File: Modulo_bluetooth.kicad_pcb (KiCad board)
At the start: 2 copper layers, 0 parts

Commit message: Layout terminado
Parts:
- added C1: 470p, Capacitors_SMD:C_0805_HandSoldering, F.Cu at (158.4, 133.3)
- added C2: 100n, Capacitors_SMD:C_0805_HandSoldering, F.Cu at (150.6, 132.5)
- added C3: 1u, Capacitors_SMD:C_0805_HandSoldering, F.Cu at (150.6, 134.6)
- added D1: 1N5817, w_smd_diode:do214ac, F.Cu at (156.1, 139.3)
- added D2: LED, LEDs:LED_0805, F.Cu at (161.7, 132.3)
- added P1: CONN_01X06, Pin_Headers:Pin_Header_Angled_1x06, F.Cu at (162.7, 142.2)
- added R1: 41k, Resistors_SMD:R_0805_HandSoldering, F.Cu at (162.1, 136.8)
- added R2: 220k, Resistors_SMD:R_0805_HandSoldering, F.Cu at (155.6, 136.8)
- added R3: 10k, Resistors_SMD:R_0805_HandSoldering, F.Cu at (162.1, 138.9)
- added R4: 2k, Resistors_SMD:R_0805_HandSoldering, F.Cu at (162.1, 134.6)
- added SW1: SW_Push, Buttons_Switches_SMD:SW_SPST_B3U-1000P-B, F.Cu at (150.6, 138.2)
- added U1: HC-05, IFS-BoB:HC-06, F.Cu at (156.3, 116.3)
- added U2: MIC5219-3.3BM5, TO_SOT_Packages_SMD:SOT-23-5, F.Cu at (155.3, 133.5)
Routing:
- net Net-(R3-Pad2): track 0.00 -> 55.8 mm, vias 0 -> 4
- net GND: track 0.00 -> 51.8 mm, vias 0 -> 6
- net STATE: track 0.00 -> 38.6 mm, vias 0 -> 1
- net TXD: track 0.00 -> 36.1 mm, vias 0 -> 1
- net RXD: track 0.00 -> 34.2 mm, vias 0 -> 1
- net Net-(R4-Pad2): track 0.00 -> 24.9 mm, vias 0 -> 2
- net +3V3: track 0.00 -> 18.8 mm
- net EN: track 0.00 -> 7.43 mm
- net Net-(R1-Pad1): track 0.00 -> 6.25 mm
- net Net-(D1-Pad1): track 0.00 -> 4.86 mm
- net +5V: track 0.00 -> 3.92 mm
- net Net-(D2-Pad2): track 0.00 -> 2.34 mm
- net Net-(C1-Pad1): track 0.00 -> 2.21 mm
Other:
- board outline added: 18.2 x 36.3 mm

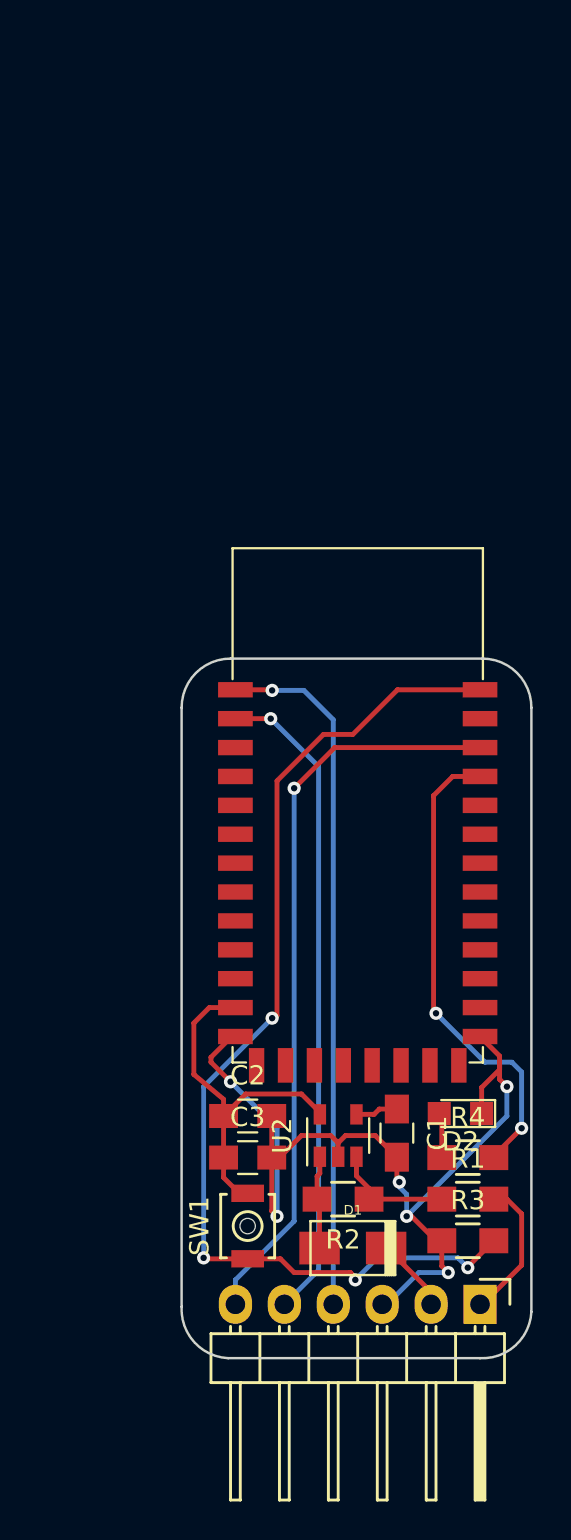
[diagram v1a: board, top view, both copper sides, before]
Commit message: Serigrafia añadida
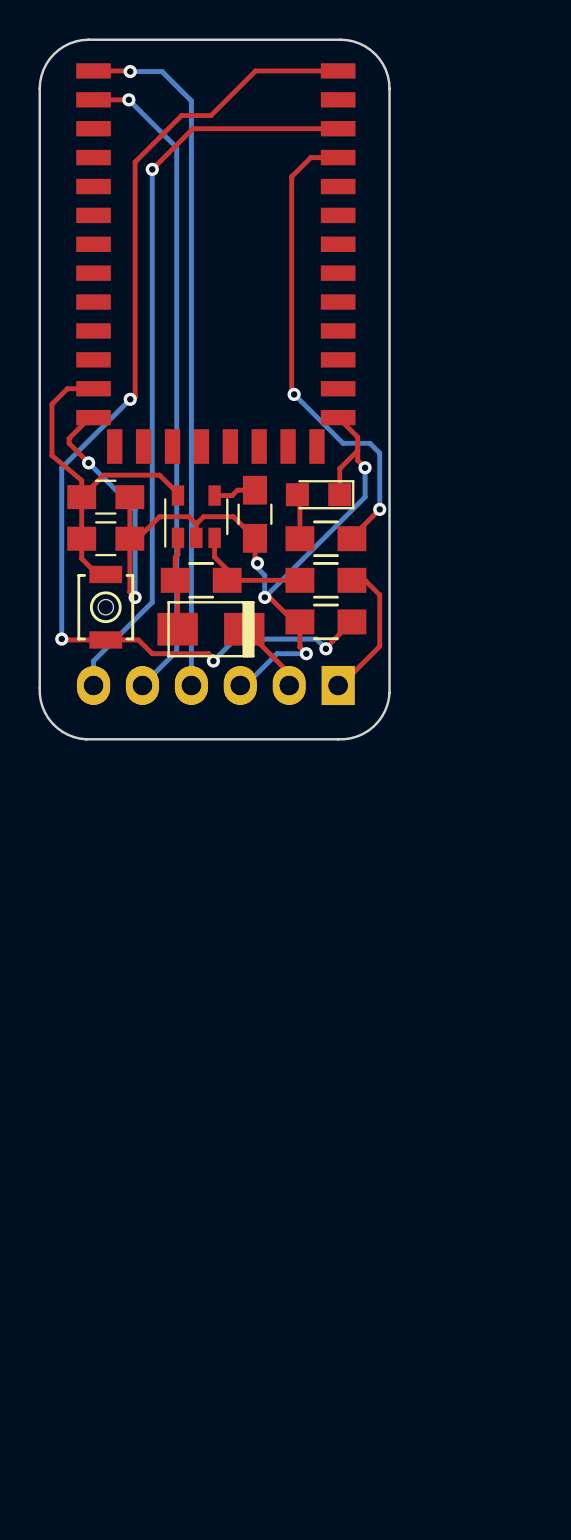
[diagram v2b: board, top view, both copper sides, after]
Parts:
- added G***: LOGO, logos_frizzy:logo_bluetooth, B.Cu at (148.8, 87.2)
- moved C2 33.0 mm to (143.3, 100.3)
- moved P1 33.0 mm to (155.3, 110.1)
- moved C1 33.0 mm to (151.0, 101.2)
- moved C3 33.0 mm to (143.3, 102.5)
- moved D2 33.0 mm to (154.3, 100.2)
- moved R1 33.0 mm to (154.7, 104.6)
- moved R2 33.0 mm to (148.2, 104.6)
- moved R4 33.0 mm to (154.7, 102.5)
- moved U1 33.0 mm to (149.0, 84.2)
- moved U2 33.0 mm to (148.0, 101.3)
- moved SW1 33.0 mm to (143.3, 106.0)
- moved D1 33.0 mm to (148.7, 107.2)
- moved R3 33.0 mm to (154.7, 106.8)
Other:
- board text added: "EN"
- board text added: "GND"
- board text added: "HC-05"
- board text added: "RX"
- board text added: "STATE"
- board text added: "TX"
- board text added: "VCC"
- board text added: "VCC: 3.6V-5V"
